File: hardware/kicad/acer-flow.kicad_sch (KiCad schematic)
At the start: 46 parts, among them J1 Conn_01x01_Socket, J2 Conn_01x01_Socket, J3 Conn_01x01_Socket, J4 Conn_01x01_Socket, J5 USB_C_Receptacle_USB2.0_16P, J6 Conn_01x04, Q1 WPM2015-3/TR, Q2 WPM2015-3/TR, SW1 RESET, SW2 USER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

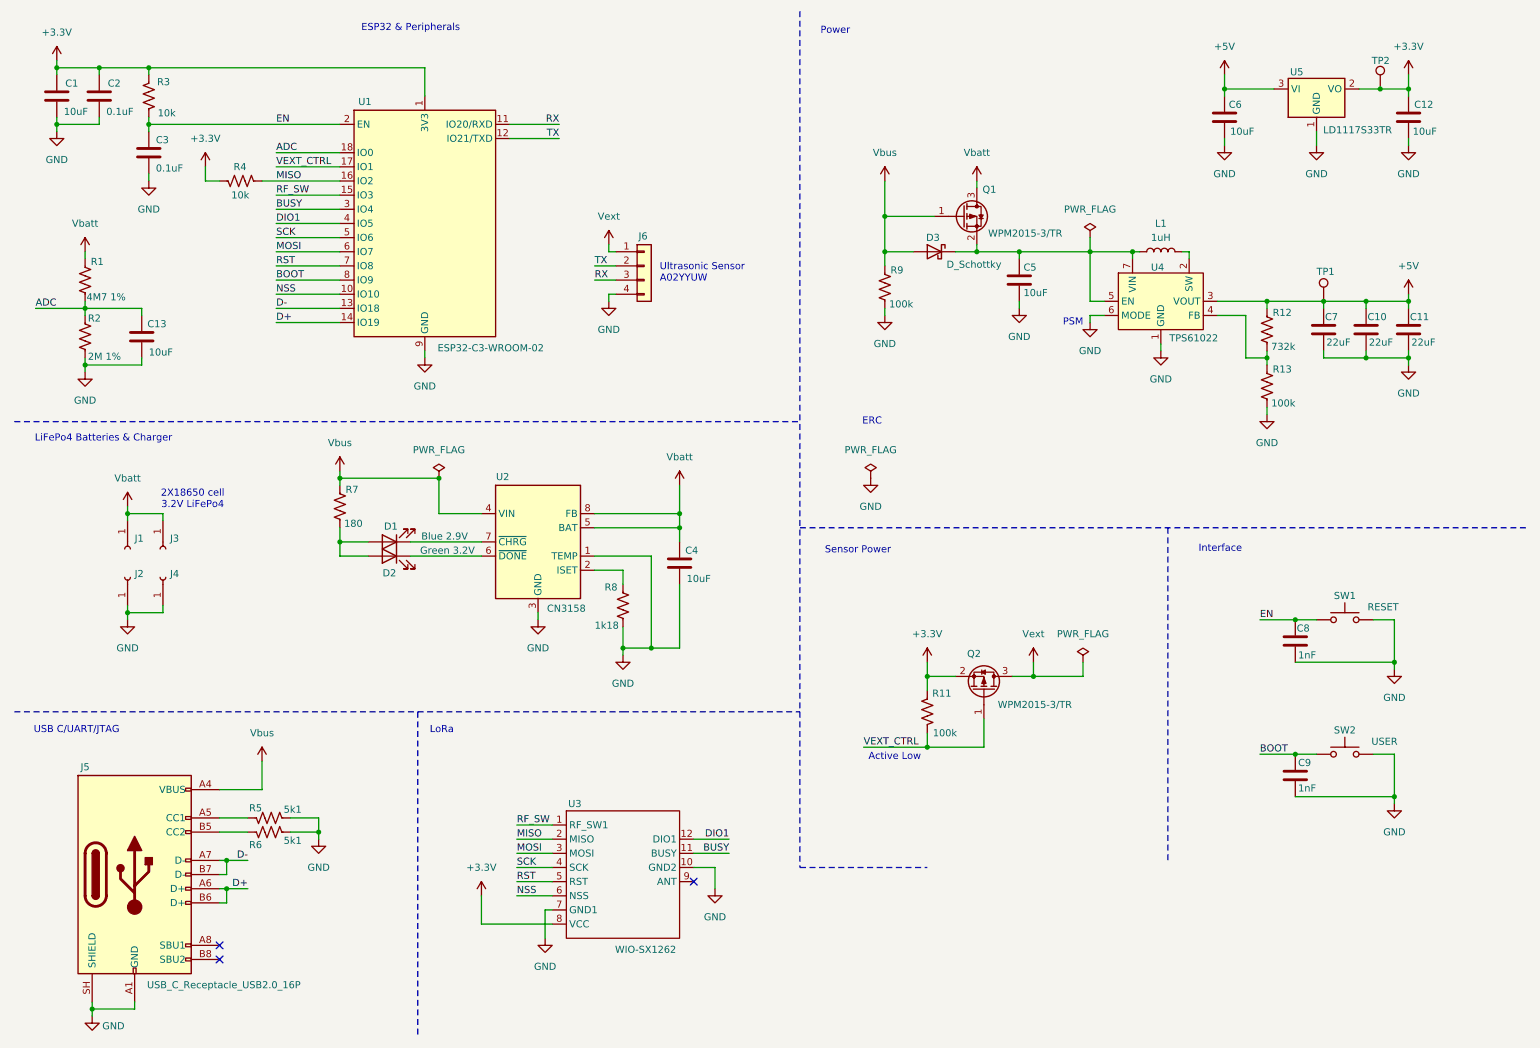
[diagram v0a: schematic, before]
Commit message: Replacing MCU ESP32 by nRF54L15
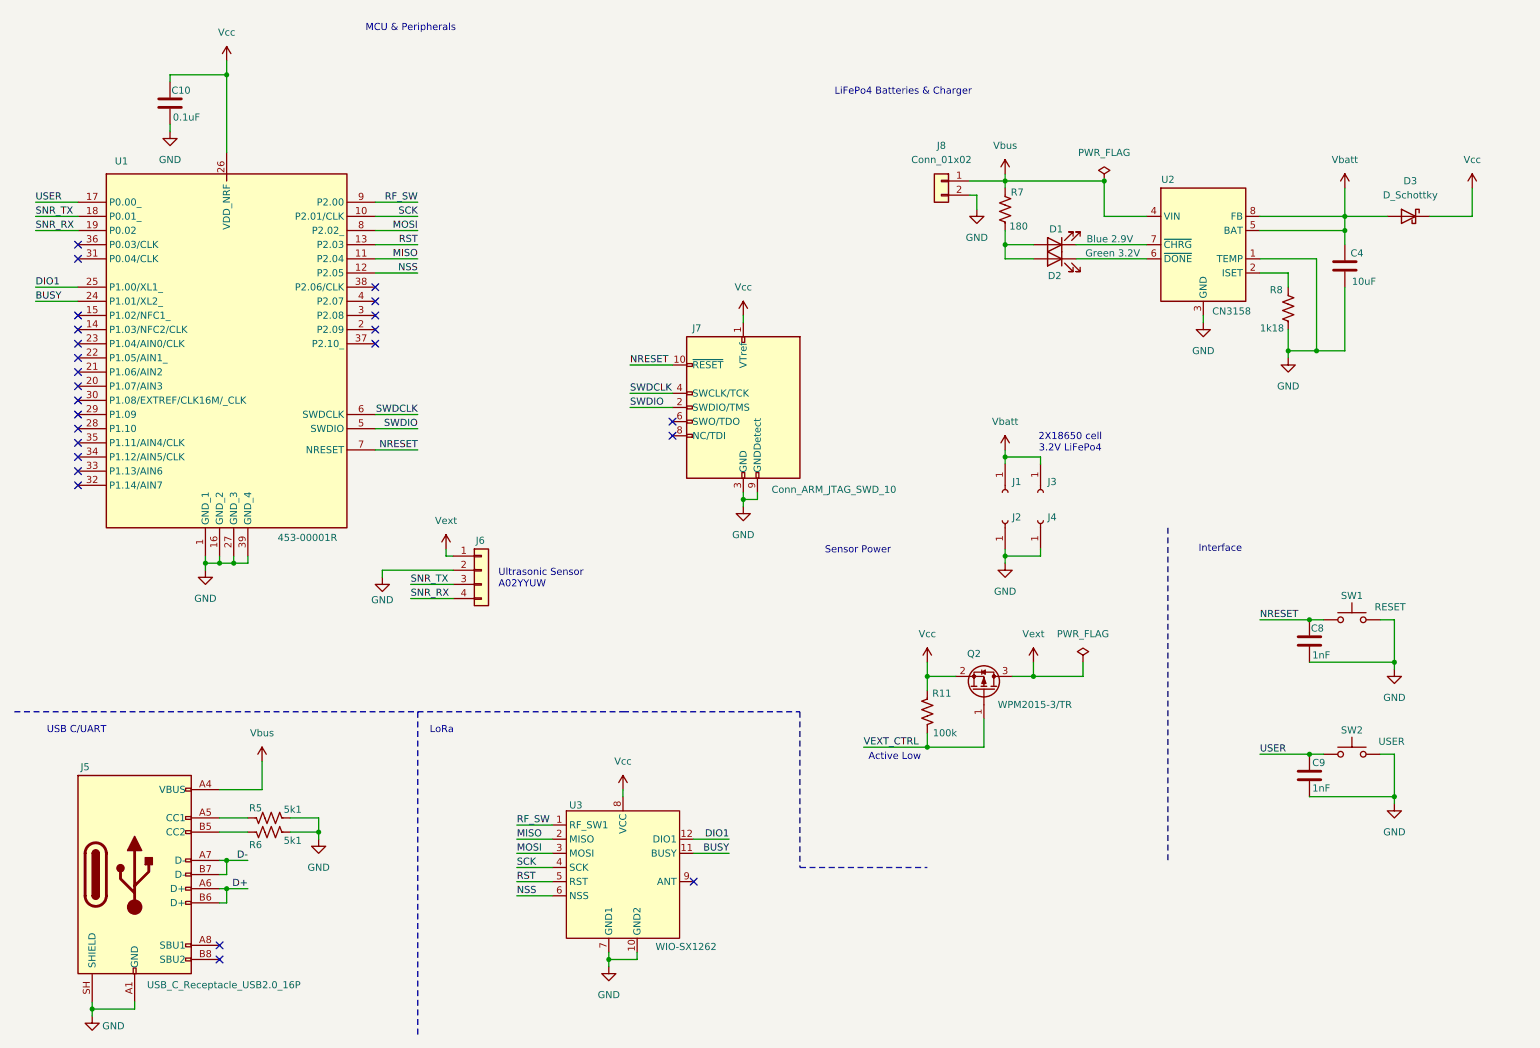
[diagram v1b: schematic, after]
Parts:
- removed C1, C12, C13, C5, C6: 10uF, Capacitor_SMD:C_0603_1608Metric, symbol Device:C
- removed C11, C7: 22uF, Capacitor_SMD:C_0603_1608Metric, symbol Device:C
- removed C2, C3: 0.1uF, Capacitor_SMD:C_0603_1608Metric, symbol Device:C
- removed L1: 1uH, symbol Device:L
- removed Q1: WPM2015-3/TR, Package_TO_SOT_SMD:SOT-23, symbol Transistor_FET:Q_PMOS_GSD
- removed R1: 4M7 1%, Resistor_SMD:R_0603_1608Metric, symbol Device:R_US
- removed R12: 732k, Resistor_SMD:R_0603_1608Metric, symbol Device:R_US
- removed R13, R9: 100k, Resistor_SMD:R_0603_1608Metric, symbol Device:R_US
- removed R2: 2M 1%, Resistor_SMD:R_0603_1608Metric, symbol Device:R_US
- removed R3, R4: 10k, Resistor_SMD:R_0603_1608Metric, symbol Device:R_US
- removed TP1, TP2: TestPoint, TestPoint:TestPoint_Pad_D1.5mm, symbol Connector:TestPoint
- removed U1: ESP32-C3-WROOM-02, RF_Module:ESP32-C3-WROOM-02, symbol RF_Module:ESP32-C3-WROOM-02
- removed U3: WIO-SX1262, symbol Wio-SX1262 Schematic Package:MODULE-WIO-SX1262
- removed U4: TPS61022, Package_DFN_QFN:Texas_RWU0007A_VQFN-7_2x2mm_P0.5mm, symbol Converter_DCDC:TPS61022
- removed U5: LD1117S33TR, Package_TO_SOT_SMD:SOT-223-3_TabPin2, symbol Regulator_Linear:LD1117S33TR_SOT223
- added J7: Conn_ARM_JTAG_SWD_10, symbol Connector:Conn_ARM_JTAG_SWD_10
- added J8: Conn_01x02, symbol Connector_Generic:Conn_01x02
- added U1: 453-00001R, SB-Lib:45300001R, symbol SB-Lib:453-00001R-SB
- added U3: WIO-SX1262, SB-Lib:Wio-SX1262-SB, symbol SB-Lib:MODULE-WIO-SX1262-SB
- C10: value 22uF -> 0.1uF
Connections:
- net +3.3V is gone; now on net Vcc: Q2.2 (S), R11.1
- net +5V is gone; now on net Vcc: C10.1
- net TX is gone; now on net GND: J6.2 (Pin_2)
- net BUSY: now also U1.24 (P1.01/XL2_), U3.11 (BUSY)
- net DIO1: now also U1.25 (P1.00/XL1_), U3.12 (DIO1)
- net GND: now also J7.3 (GND), J7.5 (GND), J7.9 (GNDDetect), J8.2 (Pin_2), U1.1 (GND_1), U1.16 (GND_2), U1.27 (GND_3), U1.39 (GND_4), U3.10 (GND2), U3.7 (GND1); no longer J6.4 (Pin_4)
- net MISO: now also U1.11 (P2.04), U3.2 (MISO)
- net MOSI: now also U1.8 (P2.02_), U3.3 (MOSI)
- net NSS: now also U1.12 (P2.05), U3.6 (NSS)
- net RF_SW: now also U1.9 (P2.00), U3.1 (RF_SW1)
- net RST: now also U1.13 (P2.03), U3.5 (RST)
- net SCK: now also U1.10 (P2.01/CLK), U3.4 (SCK)
- net Vbatt: now also D3.2 (A)
- net Vbus: now also J8.1 (Pin_1); no longer D3.2 (A)
- net Vcc: now reaches D3.1 (K)
- net Vcc: now also J7.1 (VTref), U1.26 (VDD_NRF), U3.8 (VCC)
- net BOOT renamed USER
- net USER: now also U1.17 (P0.00_)
- net EN renamed NRESET
- net NRESET: now also J7.10 (~{RESET}), U1.7 (NRESET)
- net RX renamed SNR_TX
- net SNR_TX: now also U1.18 (P0.01_)
- new net SNR_RX: J6.4 (Pin_4), U1.19 (P0.02)
- new net SWDCLK: J7.4 (SWCLK/TCK), U1.6 (SWDCLK)
- new net SWDIO: J7.2 (SWDIO/TMS), U1.5 (SWDIO)
- no-connect marks 3 -> 25
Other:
- note added: "MCU & Peripherals"
- note added: "USB C/UART"
- note removed: "ERC"
- note removed: "ESP32 & Peripherals"
- note removed: "PSM"
- note removed: "Power"
- note removed: "USB C/UART/JTAG"
- moved on the sheet: C4, C8, C9, D1, D2, J1, J2, J3, J4, J6, R7, R8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

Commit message: Adding footprints. Starting layout
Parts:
- removed C4: 10uF, Capacitor_SMD:C_0603_1608Metric, symbol Device:C
- removed D1: Blue 2.9V, symbol Device:LED
- removed D2: Green 3.2V, symbol Device:LED
- removed D3: D_Schottky, symbol Device:D_Schottky
- removed J1, J2, J3, J4: Conn_01x01_Socket, symbol Connector:Conn_01x01_Socket
- removed J5: USB_C_Receptacle_USB2.0_16P, symbol Connector:USB_C_Receptacle_USB2.0_16P
- removed J7: Conn_ARM_JTAG_SWD_10, symbol Connector:Conn_ARM_JTAG_SWD_10
- removed J8: Conn_01x02, symbol Connector_Generic:Conn_01x02
- removed Q2: WPM2015-3/TR, Package_TO_SOT_SMD:SOT-23, symbol Transistor_FET:Q_PMOS_GSD
- removed R11: 100k, Resistor_SMD:R_0603_1608Metric, symbol Device:R_US
- removed R5, R6: 5k1, Resistor_SMD:R_0603_1608Metric, symbol Device:R_US
- removed R7: 180, Resistor_SMD:R_0603_1608Metric, symbol Device:R_US
- removed R8: 1k18, Resistor_SMD:R_0603_1608Metric, symbol Device:R_US
- removed U2: CN3158, Package_SO:SOIC-8-1EP_3.9x4.9mm_P1.27mm_EP2.41x3.3mm_ThermalVias, symbol Battery_Management:CN3158
- added C2: 100nF, Capacitor_SMD:C_0603_1608Metric, symbol Device:C
- added J1: Conn_01x03, Connector_PinHeader_2.54mm:PinHeader_1x03_P2.54mm_Vertical, symbol Connector_Generic:Conn_01x03
- added J2: Conn_01x03, Connector_JST:JST_XH_B3B-XH-A_1x03_P2.50mm_Vertical, symbol Connector_Generic:Conn_01x03
- added J3: JTAG / SWD, Connector_PinHeader_1.27mm:PinHeader_2x05_P1.27mm_Vertical_SMD, symbol Connector_Generic:Conn_02x05_Odd_Even
- added Q1: AO3401A, Package_TO_SOT_SMD:SOT-23, symbol Transistor_FET:AO3401A
- added R1: 4K7, Resistor_SMD:R_0603_1608Metric, symbol Device:R_US
- added R2: 100, Resistor_SMD:R_0603_1608Metric, symbol Device:R_US
- added R3: 100K, Resistor_SMD:R_0603_1608Metric, symbol Device:R_US
- J4: renamed from J6; footprint (none) -> Connector_JST:JST_XH_B4B-XH-A_1x04_P2.50mm_Vertical
- SW1, SW2: footprint (none) -> Button_Switch_THT:SW_PUSH_6mm
- renumbered C10 to C1, C8 to C3, C9 to C4, U3 to U1, U1 to U2
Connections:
- net GND: now also C2.2, J1.3 (Pin_3), J2.3 (Pin_3), J3.3 (Pin_3), J3.5 (Pin_5), J3.9 (Pin_9)
- net NRESET: now also J3.10 (Pin_10)
- net SWDCLK: now also J3.4 (Pin_4)
- net SWDIO: now also J3.2 (Pin_2)
- net Vext: now also J2.1 (Pin_1), Q1.3 (D), R1.1
- net TEMP_DATA: now reaches U2.14 (P1.03/NFC2/CLK)
- net TEMP_DATA: now also C2.1, J2.2 (Pin_2), R1.2
- net VEXT_EN: now reaches U2.15 (P1.02/NFC1_)
- net VEXT_EN: now also R2.1
- net TXD: now reaches U2.3 (P2.08)
- net TXD: now also J1.2 (Pin_2)
- net RXD: now reaches U2.4 (P2.07)
- net RXD: now also J1.1 (Pin_1)
- net Vcc renamed +3.3V
- net +3.3V: now also J3.1 (Pin_1), Q1.2 (S), R3.1
- new net: Q1.1 (G), R2.2, R3.2
- no-connect marks 25 -> 20
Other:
- note added: "Debug"
- note added: "Sensors"
- note added: "Serial Port"
- note added: "Temperature Sensor DS18B20 1-Wire"
- note added: "Ultrasonic Sensor A02YYUW Serial"
- note removed: "2X18650 cell 3.2V LiFePo4"
- note removed: "LiFePo4 Batteries & Charger"
- note removed: "Sensor Power"
- note removed: "USB C/UART"
- note removed: "Ultrasonic Sensor A02YYUW"
- title: AcerFlow Ultrasonic Water Level -> MCU
- moved on the sheet: C1, C3, C4, J4, SW1, SW2, U1, U2
